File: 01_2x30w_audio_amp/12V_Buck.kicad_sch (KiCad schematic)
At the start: 19 parts, among them Q201 AON7534, U201 AP64500

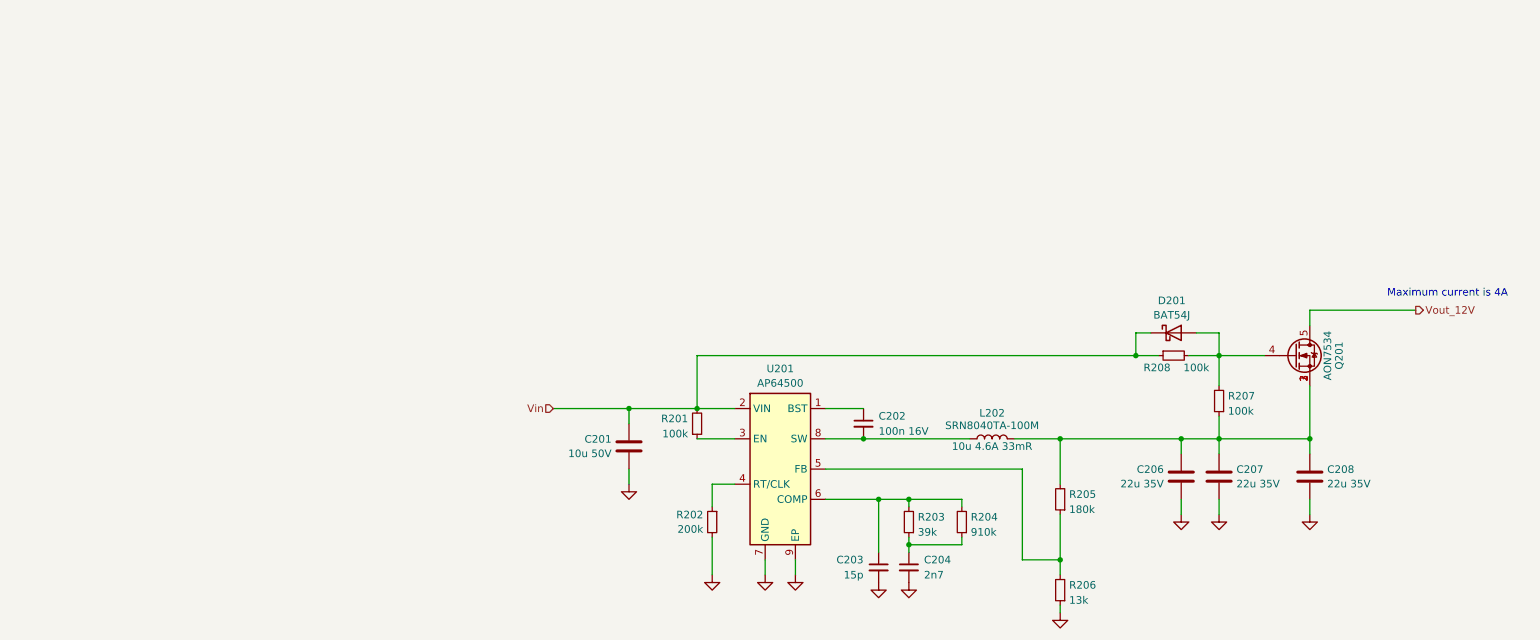
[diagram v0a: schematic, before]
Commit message: Module no. 1 completely redesigned
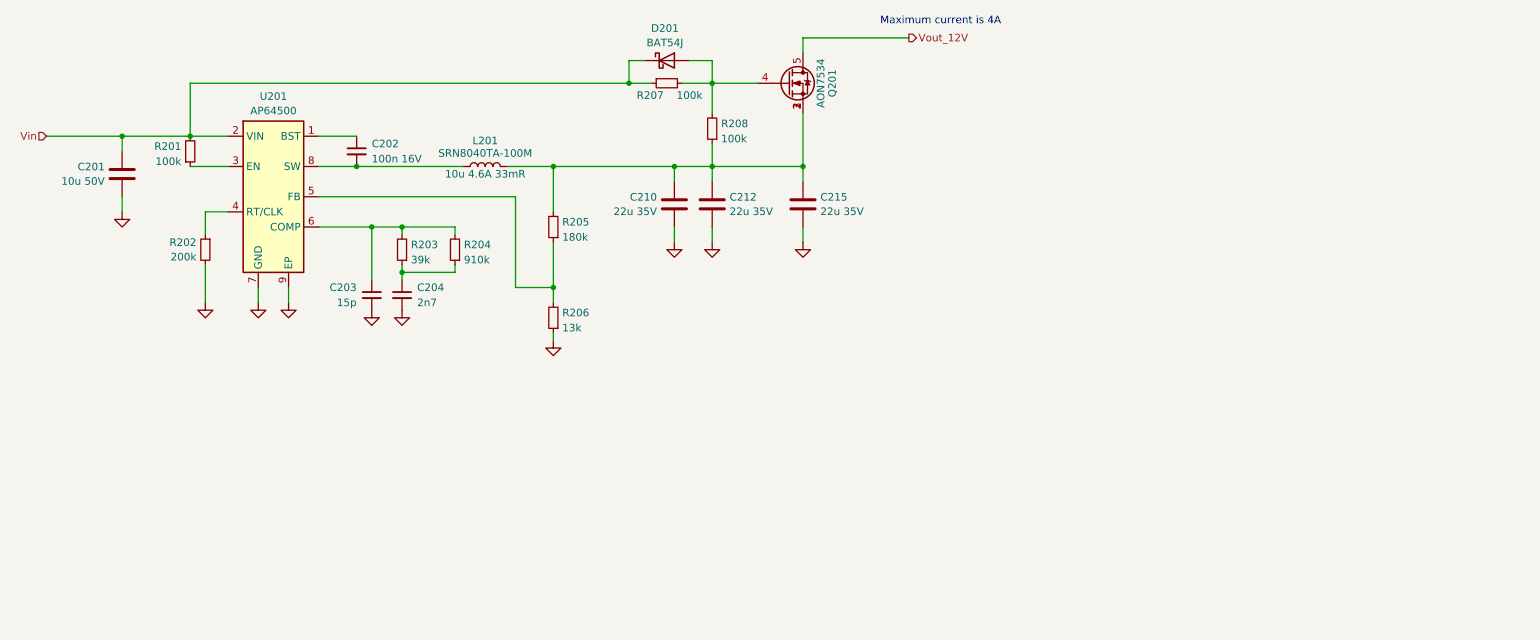
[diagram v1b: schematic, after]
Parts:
- renumbered C206 to C210, C207 to C212, C208 to C215, L202 to L201, R208 to R207, R207 to R208
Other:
- moved on the sheet: C201, C202, C203, C204, C210, C212, C215, D201, L201, Q201, R201, R202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
